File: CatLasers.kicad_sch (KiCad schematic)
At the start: 8 parts, among them J2 Programmer, J3 Conn_01x04, J4 IR Emitter, J5 Conn_01x20, J6 Conn_01x04, U2 ESP32-WROOM-32E_(4MB_HIGH_TEM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

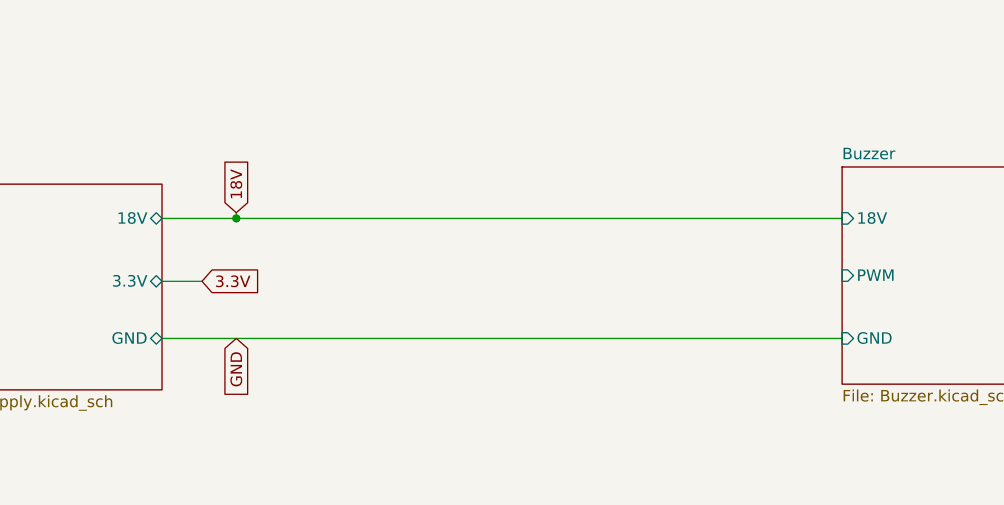
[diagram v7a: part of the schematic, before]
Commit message: Added power jumper
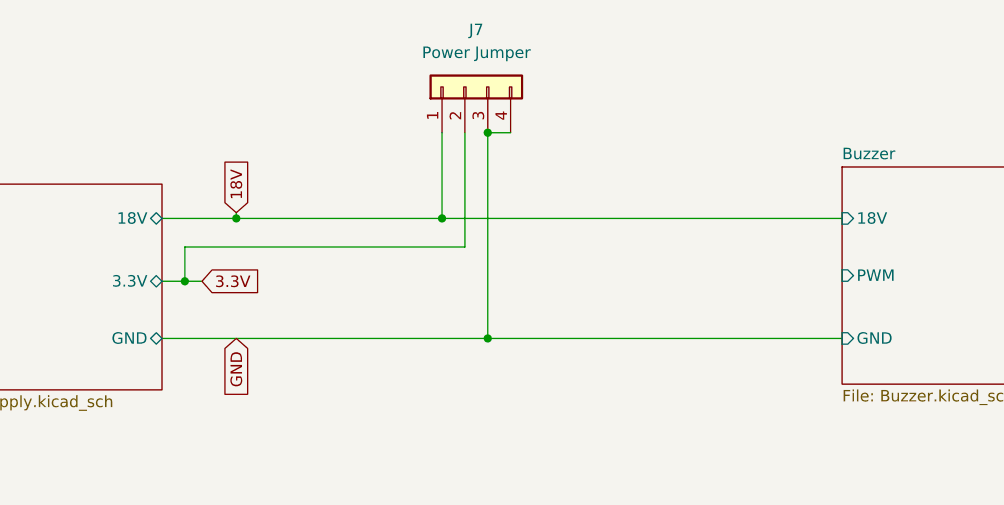
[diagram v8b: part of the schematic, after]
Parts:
- added J7: Power Jumper, Connector_PinHeader_2.54mm:PinHeader_1x04_P2.54mm_Vertical, symbol Connector_Generic:Conn_01x04
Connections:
- net 18V: now also J7.1 (Pin_1)
- net 3.3V: now also J7.2 (Pin_2)
- net GND: now also J7.3 (Pin_3), J7.4 (Pin_4)
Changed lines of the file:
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@@
   (junction (at 80.645 42.545) (diameter 0) (color 0 0 0 0)
   )
+  (junction (at 74.93 49.53) (diameter 0) (color 0 0 0 0)
+  )
+  (junction (at 108.585 55.88) (diameter 0) (color 0 0 0 0)
+  )
   (junction (at 179.705 101.6) (diameter 0) (color 0 0 0 0)
   )
+  (junction (at 103.505 42.545) (diameter 0) (color 0 0 0 0)
+  )
+  (junction (at 108.585 33.02) (diameter 0) (color 0 0 0 0)
+  )
   (junction (at 64.77 153.67) (diameter 0) (color 0 0 0 0)
   )
@@
     (stroke (width 0) (type default))
   )
+  (wire (pts (xy 108.585 33.02) (xy 111.125 33.02))
+    (stroke (width 0) (type default))
+  )
   (wire (pts (xy 105.41 99.06) (xy 109.22 99.06))
     (stroke (width 0) (type default))
@@
     (stroke (width 0) (type default))
   )
+  (wire (pts (xy 106.045 45.72) (xy 106.045 33.02))
+    (stroke (width 0) (type default))
+  )
   (wire (pts (xy 109.22 139.7) (xy 105.41 139.7))
     (stroke (width 0) (type default))
@@
     (stroke (width 0) (type default))
   )
+  (wire (pts (xy 74.93 49.53) (xy 74.93 45.72))
+    (stroke (width 0) (type default))
+  )
+  (wire (pts (xy 108.585 55.88) (xy 147.955 55.88))
+    (stroke (width 0) (type default))
+  )
   (wire (pts (xy 45.72 99.06) (xy 45.72 116.205))
     (stroke (width 0) (type default))
@@
     (stroke (width 0) (type default))
   )
+  (wire (pts (xy 103.505 33.02) (xy 103.505 42.545))
+    (stroke (width 0) (type default))
+  )
   (wire (pts (xy 64.77 111.76) (xy 62.23 111.76))
     (stroke (width 0) (type default))
@@
     (stroke (width 0) (type default))
   )
-  (wire (pts (xy 72.39 49.53) (xy 76.835 49.53))
-    (stroke (width 0) (type default))
-  )
-  (wire (pts (xy 80.645 42.545) (xy 147.955 42.545))
+  (wire (pts (xy 72.39 49.53) (xy 74.93 49.53))
+    (stroke (width 0) (type default))
+  )
+  (wire (pts (xy 80.645 42.545) (xy 103.505 42.545))
     (stroke (width 0) (type default))
   )
@@
     (stroke (width 0) (type default))
   )
+  (wire (pts (xy 74.93 45.72) (xy 106.045 45.72))
+    (stroke (width 0) (type default))
+  )
   (wire (pts (xy 109.22 114.3) (xy 105.41 114.3))
     (stroke (width 0) (type default))
@@
     (stroke (width 0) (type default))
   )
+  (wire (pts (xy 74.93 49.53) (xy 76.835 49.53))
+    (stroke (width 0) (type default))
+  )
   (wire (pts (xy 64.77 129.54) (xy 40.64 129.54))
     (stroke (width 0) (type default))
@@
     (stroke (width 0) (type default))
   )
+  (wire (pts (xy 108.585 33.02) (xy 108.585 55.88))
+    (stroke (width 0) (type default))
+  )
   (wire (pts (xy 109.22 147.32) (xy 105.41 147.32))
     (stroke (width 0) (type default))
@@
     (stroke (width 0) (type default))
   )
-  (wire (pts (xy 72.39 55.88) (xy 147.955 55.88))
+  (wire (pts (xy 72.39 55.88) (xy 108.585 55.88))
     (stroke (width 0) (type default))
   )
@@
   )
   (wire (pts (xy 64.77 151.13) (xy 64.77 153.67))
+    (stroke (width 0) (type default))
+  )
+  (wire (pts (xy 103.505 42.545) (xy 147.955 42.545))
     (stroke (width 0) (type default))
   )
@@
         )
       )
+    )
+  )
+  (symbol (lib_id "Connector_Generic:Conn_01x04") (at 106.045 27.94 90) (unit 1)
+    (in_bom yes) (on_board yes) (dnp no) (fields_autoplaced)
+    (property "Reference" "J7" (at 107.315 21.59 90)
+      (effects (font (size 1.27 1.27)))
+    )
+    (property "Value" "Power Jumper" (at 107.315 24.13 90)
+      (effects (font (size 1.27 1.27)))
+    )
+    (property "Footprint" "Connector_PinHeader_2.54mm:PinHeader_1x04_P2.54mm_Vertical" (at 106.045 27.94 0)
+      (effects (font (size 1.27 1.27)) hide)
+    )
+    (property "Datasheet" "~" (at 106.045 27.94 0)
+      (effects (font (size 1.27 1.27)) hide)
+    )
+    (pin "1")
+    (pin "2")
+    (pin "3")
+    (pin "4")
+    (instances
+      (project "CatLasers"
+        (path "/b94f5b10-ee0c-4425-b025-e3a8bb3cc7b0"
+          (reference "J7") (unit 1)
+        )
+      )
